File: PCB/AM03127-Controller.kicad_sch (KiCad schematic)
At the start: 12 parts, among them U1 XIAO-ESP32-C3-DIP, U2 MAX3232, U3 AMS1117

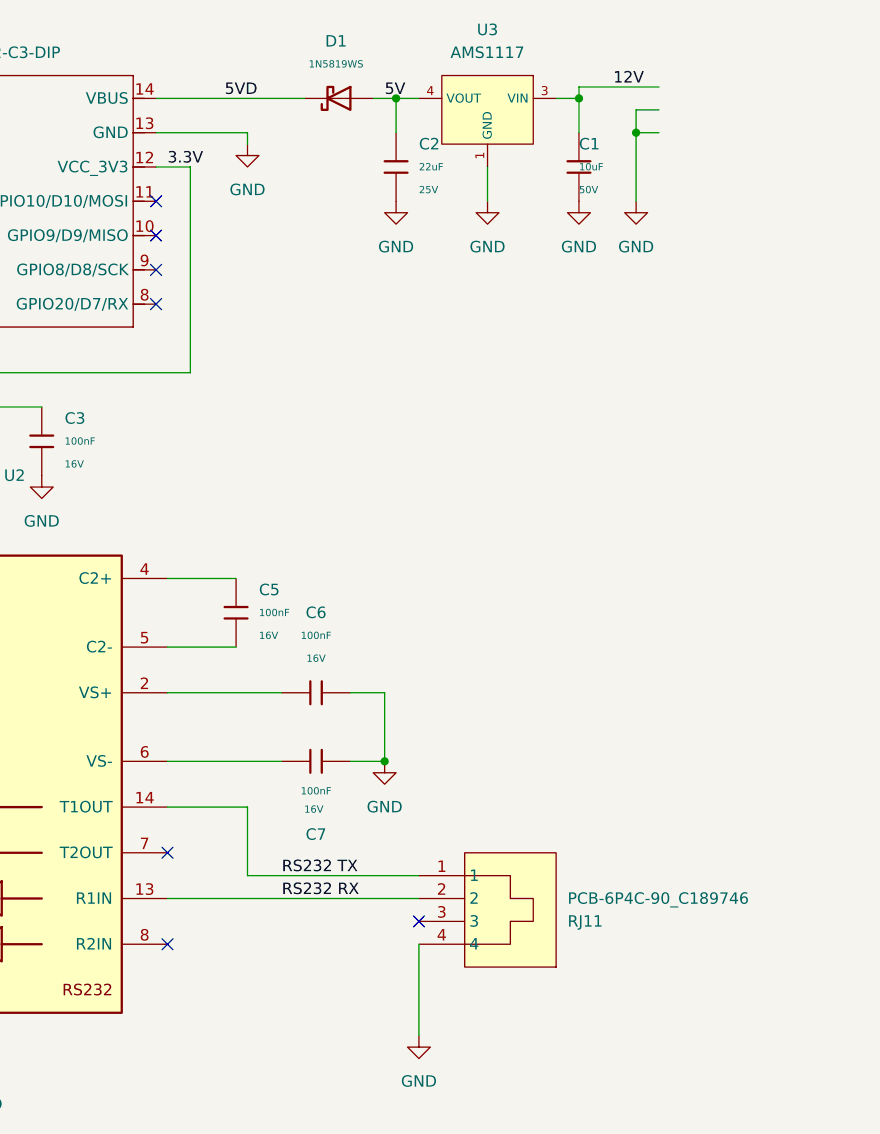
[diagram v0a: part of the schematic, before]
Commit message: Restructure PCB project
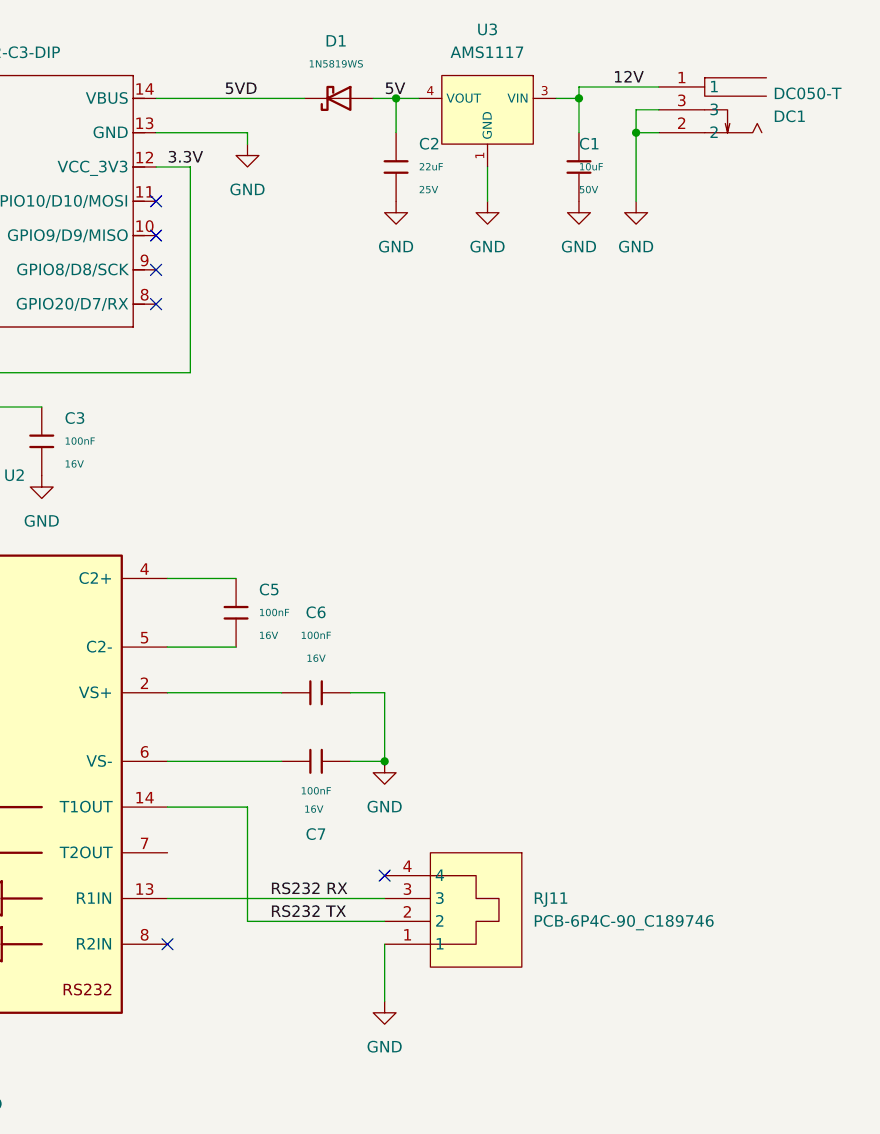
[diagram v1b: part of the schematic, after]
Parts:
- added DC1: DC050-T, DC_PowerJack:DC-IN_DC050-T, symbol DC_PowerJack:DC050-T
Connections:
- net 12V: now also DC1.1
- net GND: now also RJ11.1, DC1.2, DC1.3; no longer RJ11.4
- net RS232 RX: now also RJ11.3; no longer RJ11.2
- net RS232 TX: now also RJ11.2; no longer RJ11.1
- no-connect marks 14 -> 13
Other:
- moved on the sheet: RJ11
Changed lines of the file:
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@@
 	)
 	(no_connect
+		(at 146.05 125.73)
+	)
+	(no_connect
 		(at 120.65 62.23)
 	)
@@
 	)
 	(no_connect
-		(at 121.92 123.19)
-	)
-	(no_connect
-		(at 149.86 130.81)
-	)
-	(no_connect
 		(at 82.55 46.99)
 	)
@@
 	(wire
 		(pts
-			(xy 124.46 46.99) (xy 124.46 69.85)
+			(xy 146.05 133.35) (xy 146.05 139.7)
 		)
 		(stroke
@@
 	(wire
 		(pts
-			(xy 101.6 73.66) (xy 101.6 85.09)
+			(xy 130.81 130.81) (xy 146.05 130.81)
 		)
 		(stroke
@@
 	(wire
 		(pts
-			(xy 121.92 113.03) (xy 134.62 113.03)
+			(xy 124.46 46.99) (xy 124.46 69.85)
 		)
 		(stroke
@@
 	(wire
 		(pts
-			(xy 149.86 133.35) (xy 149.86 143.51)
+			(xy 101.6 73.66) (xy 101.6 85.09)
+		)
+		(stroke
+			(width 0)
+			(type default)
+		)
+	)
+	(wire
+		(pts
+			(xy 121.92 113.03) (xy 134.62 113.03)
 		)
 		(stroke
@@
 	(wire
 		(pts
-			(xy 121.92 105.41) (xy 134.62 105.41)
-		)
-		(stroke
-			(width 0)
-			(type default)
-		)
-	)
-	(wire
-		(pts
-			(xy 121.92 100.33) (xy 129.54 100.33)
+			(xy 121.92 128.27) (xy 146.05 128.27)
 		)
 		(stroke
@@
 	(wire
 		(pts
-			(xy 101.6 73.66) (xy 107.95 73.66)
+			(xy 121.92 105.41) (xy 134.62 105.41)
 		)
 		(stroke
@@
 	(wire
 		(pts
-			(xy 130.81 118.11) (xy 130.81 125.73)
+			(xy 121.92 100.33) (xy 129.54 100.33)
 		)
 		(stroke
@@
 	(wire
 		(pts
-			(xy 121.92 128.27) (xy 149.86 128.27)
+			(xy 101.6 73.66) (xy 107.95 73.66)
 		)
 		(stroke
@@
 	(wire
 		(pts
-			(xy 130.81 125.73) (xy 149.86 125.73)
+			(xy 157.48 46.99) (xy 157.48 50.8)
 		)
 		(stroke
@@
 	(wire
 		(pts
-			(xy 157.48 46.99) (xy 157.48 50.8)
+			(xy 130.81 118.11) (xy 130.81 130.81)
 		)
 		(stroke
@@
 	)
 	(label "RS232 RX"
-		(at 134.62 128.27 0)
+		(at 133.35 128.27 0)
 		(effects
 			(font
@@
 	)
 	(label "RS232 TX"
-		(at 134.62 125.73 0)
+		(at 133.35 130.81 0)
 		(effects
 			(font
@@
 	(symbol
 		(lib_id "RJ11:PCB-6P4C-90_C189746")
-		(at 157.48 128.27 270)
-		(mirror x)
+		(at 153.67 130.81 270)
 		(unit 1)
 		(exclude_from_sim no)
@@
 		(dnp no)
 		(property "Reference" "RJ11"
-			(at 166.37 130.8101 90)
+			(at 162.56 128.2699 90)
 			(effects
 				(font
@@
 		)
 		(property "Value" "PCB-6P4C-90_C189746"
-			(at 166.37 128.2701 90)
+			(at 162.56 130.8099 90)
 			(effects
 				(font
@@
 		)
 		(property "Footprint" "RJ11:RJ11-TH_PCB-6P4C-90_C189746"
-			(at 142.24 128.27 0)
+			(at 138.43 130.81 0)
 			(effects
 				(font
@@
 		)
 		(property "Datasheet" "https://lcsc.com/product-detail/Ethernet-Connectors-Modular-Connectors_Shenzhen-Cankemeng-PCB-6P4C-90degree-gray-Full-gold_C189746.html"
-			(at 139.7 128.27 0)
+			(at 135.89 130.81 0)
 			(effects
 				(font
@@
 		)
 		(property "Description" ""
-			(at 157.48 128.27 0)
+			(at 153.67 130.81 0)
 			(effects
 				(font
@@
 		)
 		(property "LCSC Part" "C189746"
-			(at 137.16 128.27 0)
+			(at 133.35 130.81 0)
 			(effects
 				(font
@@
 	)
 	(symbol
+		(lib_id "DC_PowerJack:DC050-T")
+		(at 179.07 40.64 0)
+		(mirror y)
+		(unit 1)
+		(exclude_from_sim no)
+		(in_bom yes)
+		(on_board yes)
+		(dnp no)
+		(property "Reference" "DC1"
+			(at 189.23 41.4001 0)
+			(effects
+				(font
+					(size 1.27 1.27)
+				)
+				(justify right)
+			)
+		)
+		(property "Value" "DC050-T"
+			(at 189.23 38.8601 0)
+			(effects
+				(font
+					(size 1.27 1.27)
+				)
+				(justify right)
+			)
+		)
+		(property "Footprint" "DC_PowerJack:DC-IN_DC050-T"
+			(at 179.07 50.8 0)
+			(effects
+				(font
+					(size 1.27 1.27)
+				)
+				(hide yes)
+			)
+		)
+		(property "Datasheet" ""
+			(at 179.07 40.64 0)
+			(effects
+				(font
+					(size 1.27 1.27)
+				)
+				(hide yes)
+			)
+		)
+		(property "Description" ""
+			(at 179.07 40.64 0)
+			(effects
+				(font
+					(size 1.27 1.27)
+				)
+				(hide yes)
+			)
+		)
+		(property "LCSC Part" "C431534"
+			(at 179.07 53.34 0)
+			(effects
+				(font
+					(size 1.27 1.27)
+				)
+				(hide yes)
+			)
+		)
+		(pin "2"
+		)
+		(pin "1"
+		)
+		(pin "3"
+		)
+		(instances
+			(project ""
+				(path "/145d96f7-bd8e-4910-9a18-e63b5a2fc40f"
+					(reference "DC1")
+					(unit 1)
+				)
+			)
+		)
+	)
+	(symbol
 		(lib_id "PCM_JLCPCB-Capacitors:1206,10uF")
 		(at 167.64 46.99 0)
@@
 	(symbol
 		(lib_id "power:GND")
-		(at 149.86 143.51 0)
+		(at 146.05 139.7 0)
 		(unit 1)
 		(exclude_from_sim no)
@@
 		(fields_autoplaced yes)
 		(property "Reference" "#PWR06"
-			(at 149.86 149.86 0)
+			(at 146.05 146.05 0)
 			(effects
 				(font
@@
 		)
 		(property "Value" "GND"
-			(at 149.86 148.59 0)
+			(at 146.05 144.78 0)
 			(effects
 				(font
@@
 		)
 		(property "Footprint" ""
-			(at 149.86 143.51 0)
+			(at 146.05 139.7 0)
 			(effects
 				(font
@@
 		)
 		(property "Datasheet" ""
-			(at 149.86 143.51 0)
+			(at 146.05 139.7 0)
 			(effects
 				(font
@@
 		)
 		(property "Description" "Power symbol creates a global label with name \"GND\" , ground"
-			(at 149.86 143.51 0)
+			(at 146.05 139.7 0)
 			(effects
 				(font

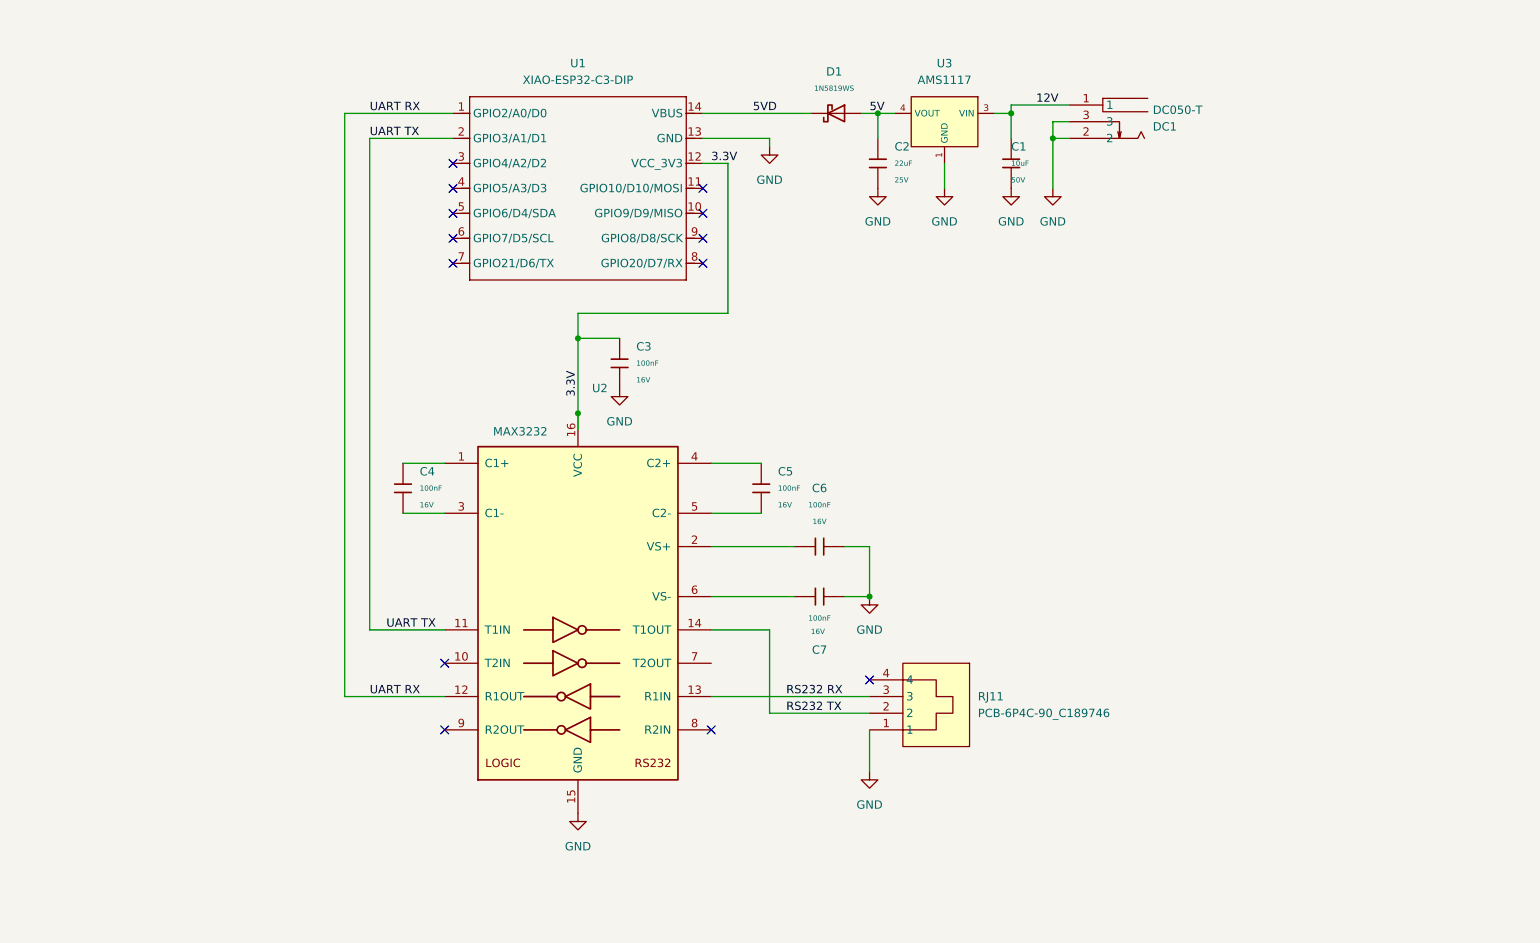
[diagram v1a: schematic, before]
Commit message: Refactor PCB to use global label  nets
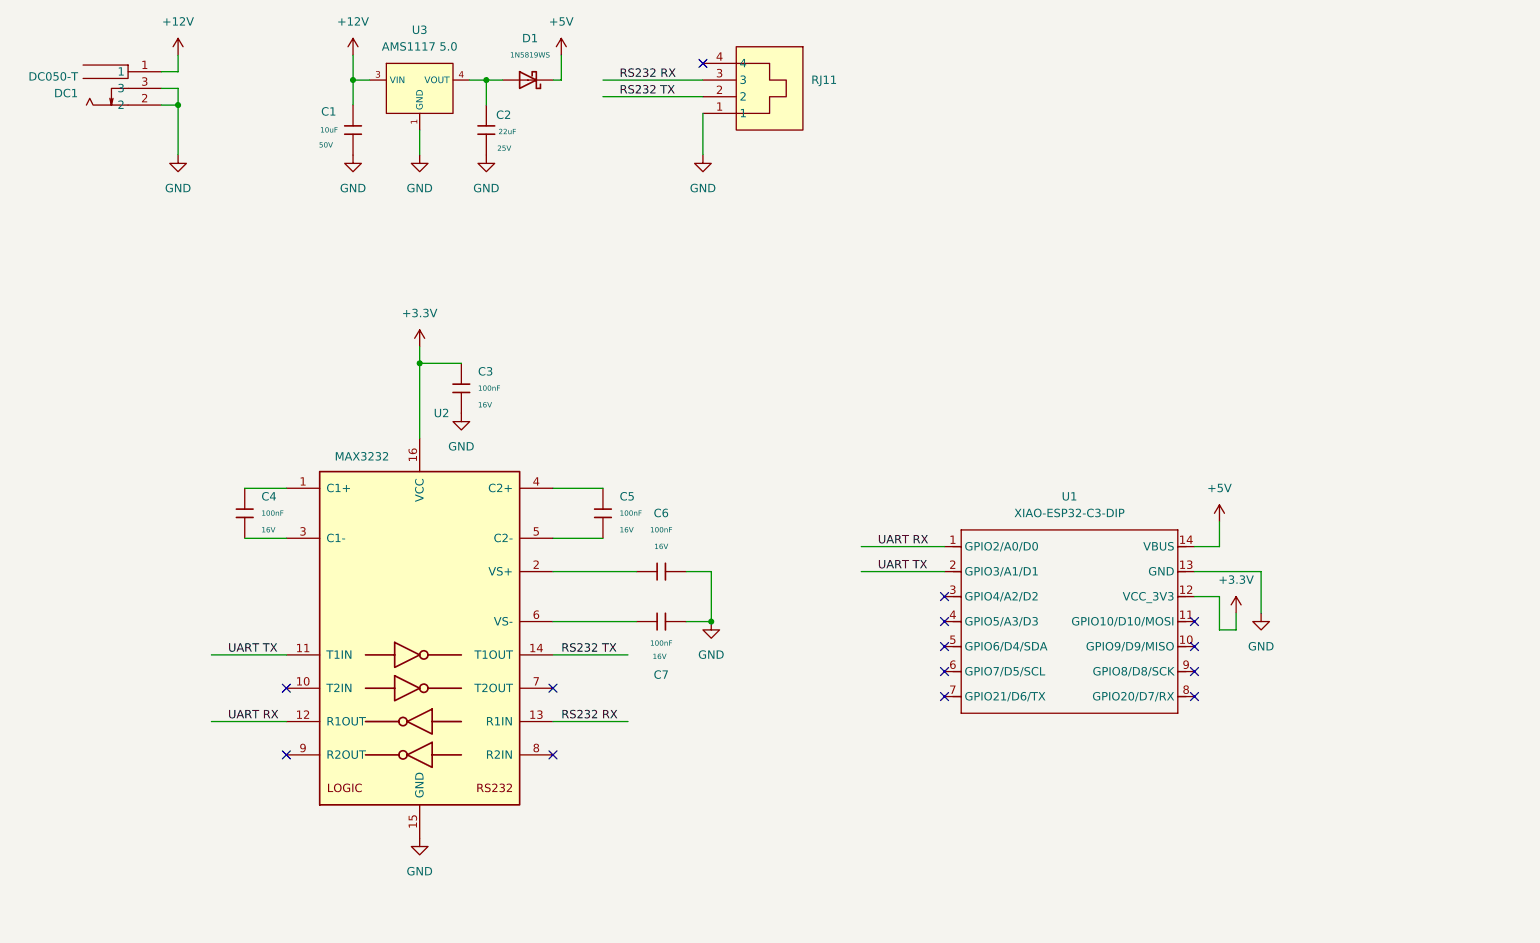
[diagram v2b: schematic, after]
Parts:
- U3: value AMS1117 -> AMS1117 5.0
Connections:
- net 12V renamed +12V
- net 3.3V renamed +3.3V
- net 5V: no longer names the net of C2.1, D1.2, U3.2 (VOUT), U3.4 (VOUT)
- net 5VD renamed +5V
- no-connect marks 13 -> 14
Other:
- title: (none) -> AM03127-Controller
- moved on the sheet: C1, C2, C3, C4, C5, C6, C7, D1, DC1, RJ11, U1, U2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

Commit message: Refactor LDO to Buckconverter
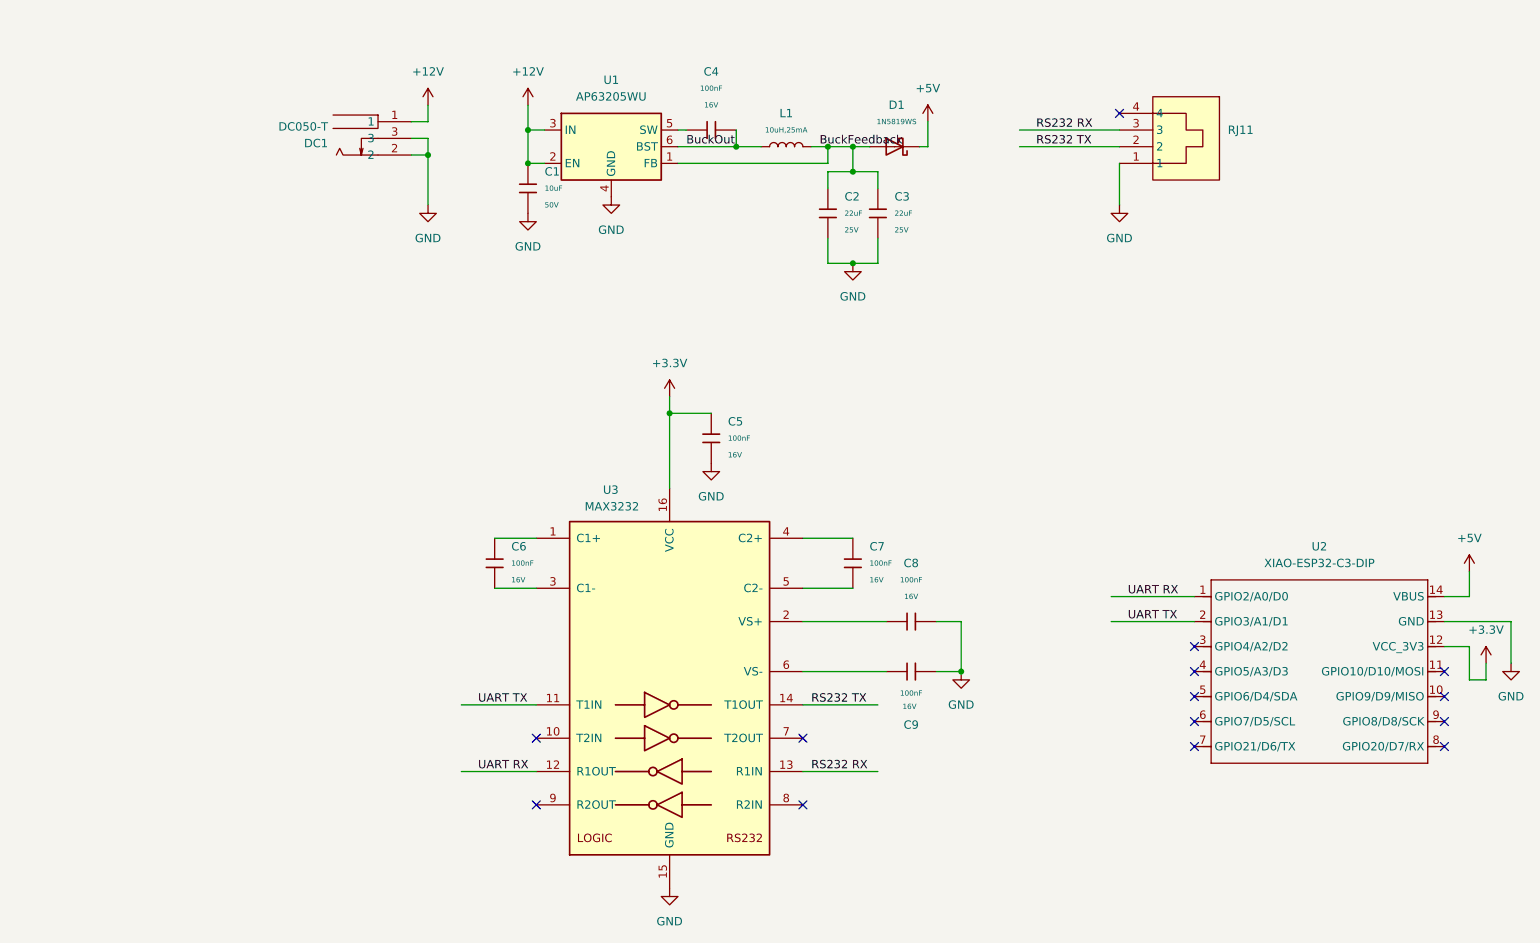
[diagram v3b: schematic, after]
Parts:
- removed C1: 10uF, PCM_JLCPCB:C_1206, symbol PCM_JLCPCB-Capacitors:1206,10uF
- removed C2: 22uF, PCM_JLCPCB:C_1206, symbol PCM_JLCPCB-Capacitors:1206,22uF,(2)
- removed U3: AMS1117 5.0, PCM_JLCPCB:SOT-223_L6.5-W3.5-P2.30-LS7.0-BR, symbol PCM_JLCPCB-Power:LDO, 5V, 1A
- added C1: 10uF, PCM_JLCPCB:C_0805, symbol PCM_JLCPCB-Capacitors:0805,10uF,(2)
- added C2, C3: 22uF, PCM_JLCPCB:C_0805, symbol PCM_JLCPCB-Capacitors:0805,22uF
- added C4: 100nF, PCM_JLCPCB:C_0402, symbol PCM_JLCPCB-Capacitors:0402,100nF
- added L1: 10uH,25mA, PCM_JLCPCB:L_1206, symbol PCM_JLCPCB-Inductors:10uH,25mA
- added U1: AP63205WU, Package_TO_SOT_SMD:TSOT-23-6, symbol Regulator_Switching:AP63205WU
- renumbered C3 to C5, C4 to C6, C5 to C7, C6 to C8, C7 to C9, U1 to U2, U2 to U3
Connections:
- net +12V: now also C1.1, U1.2 (EN), U1.3 (IN)
- net GND: now also C1.2, C2.2, C3.2, U1.4 (GND)
- net BuckFeedback: now reaches D1.2
- net BuckFeedback: now also C2.1, C3.1, L1.2, U1.1 (FB)
- new net: C4.1, U1.5 (SW)
- new net BuckOut: C4.2, L1.1, U1.6 (BST)
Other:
- moved on the sheet: C5, C6, C7, C8, C9, D1, DC1, RJ11, U2, U3
